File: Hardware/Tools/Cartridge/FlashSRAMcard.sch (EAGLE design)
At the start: 18 parts, among them IC1 AS29CF160B-55TIN, IC2 74LS595D, IC3 74LS244DW, IC5 74AHC1G04DBV, IC6 74AHC1G32DBV, IC7 74AHC1G32DBV

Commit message: more sram cart changes
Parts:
- added D1, D2: (no value), semicon-smd-ipc:D-MLL-34
- added R1, R2, R3: (no value), rcl:R-US_R0805
- added U$3: BATTERY2025-SMD, 0_gametankparts:BATTERY2025-SMD
- IC2: value 74LS595D -> 74HC595; device 74xx-us:74LS595D -> 0_gametankparts:74HC595
- IC3: value 74LS244DW -> 74HC244; device 74xx-us:74LS244DW -> 0_gametankparts:74HC244
- U$2: value SRAM_32KSOP28 -> SRAM_32KTSOP28; device 0_gametankparts:SRAM_32KSOP28 -> 0_gametankparts:SRAM_32KTSOP28
- renumbered VCC to IC4
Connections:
- new net N$5: D1.A, U$3.+
- new net N$6: C4.1, D1.C, D2.C, R1.1, R2.1, R3.1, U$2G$2.VCC
- net !OE: now also R1.2
- net !WE: now also R2.2
- net D0: now also U$2G$1.D0
- net D1: now also U$2G$1.D1
- net D2: now also U$2G$1.D2
- net D3: now also U$2G$1.D3
- net D4: now also U$2G$1.D4
- net D5: now also U$2G$1.D5
- net D6: now also U$2G$1.D6
- net D7: now also U$2G$1.D7
- net GND: now also U$1G$2.GND, U$2G$2.GND, U$3.-
- net N$2: now also R3.2
- net VCC: now also D2.A, U$1G$2.VCC; no longer C4.1
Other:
- moved on the sheet: C4, IC6

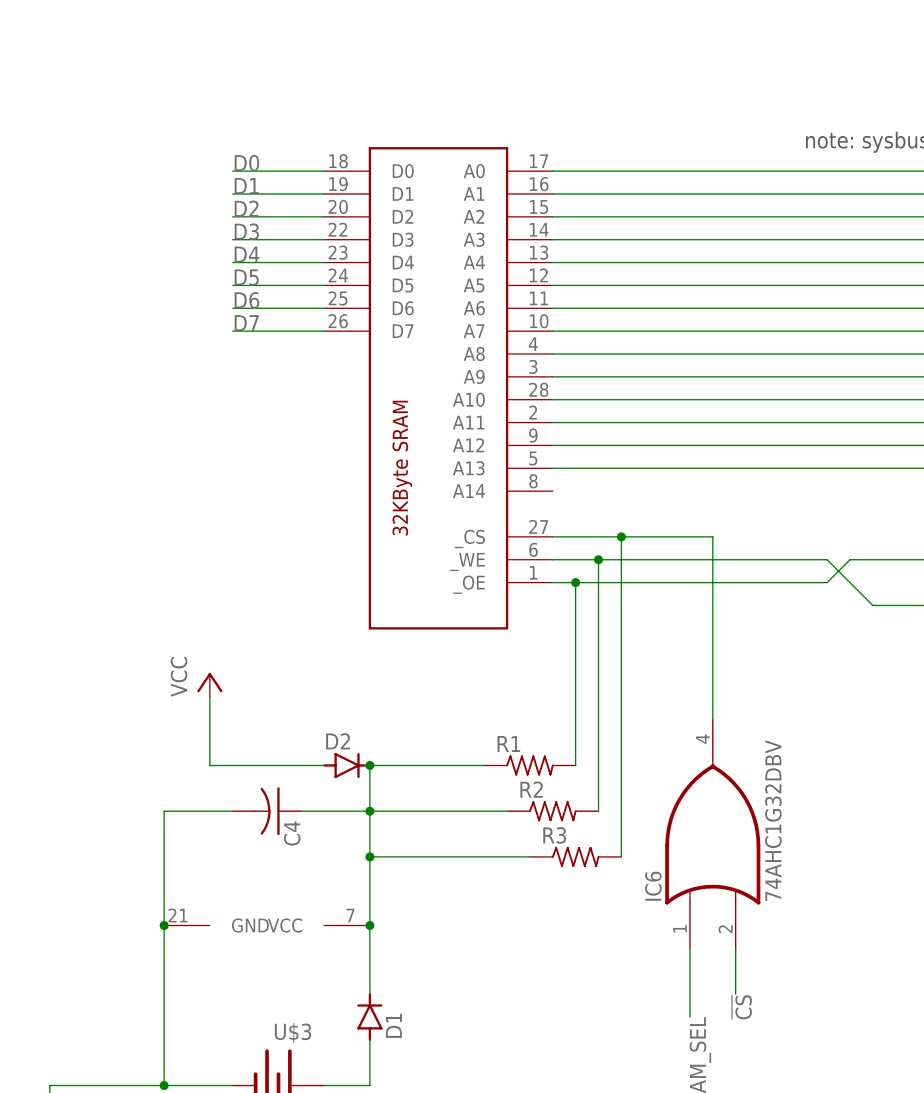
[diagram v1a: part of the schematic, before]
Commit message: RAM cartridge fixes
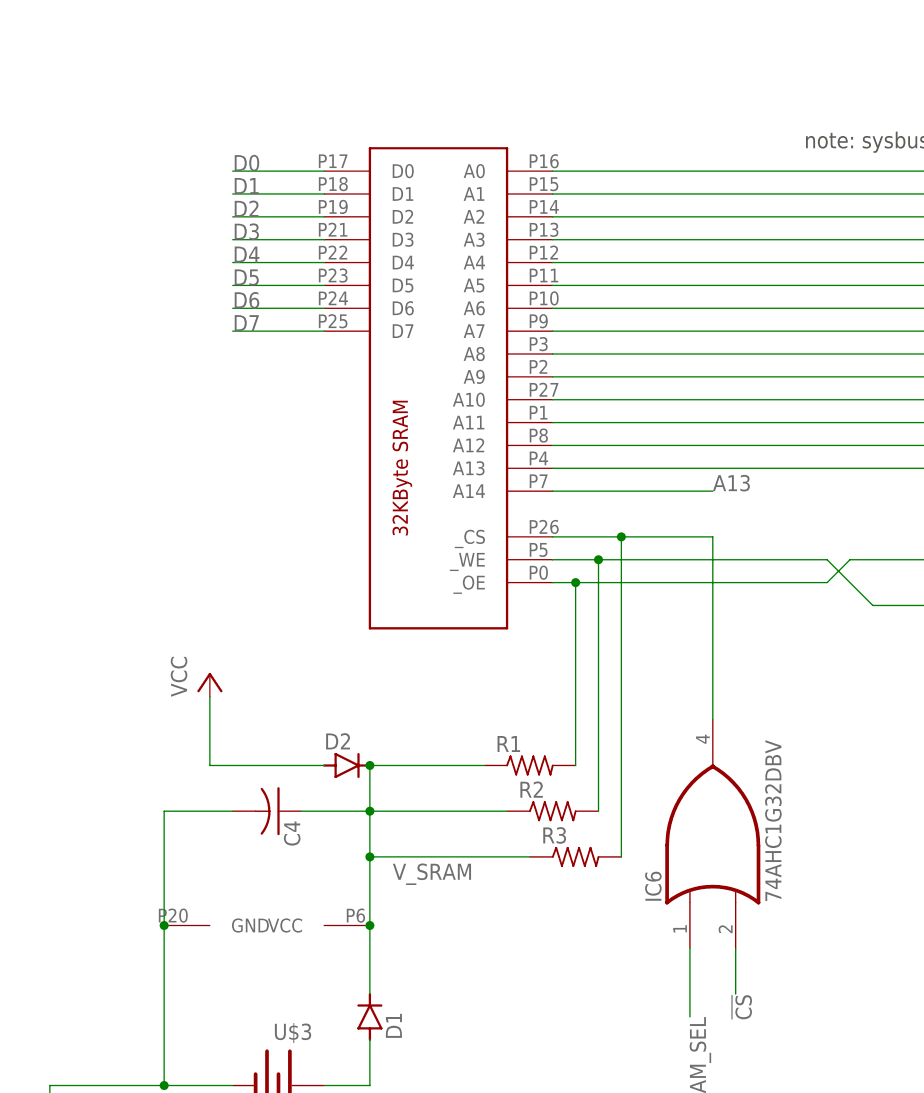
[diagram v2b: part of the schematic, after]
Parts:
- U$2: value SRAM_32KTSOP28 -> SRAM_32KALLIANCE; device 0_gametankparts:SRAM_32KTSOP28 -> 0_gametankparts:SRAM_32KALLIANCE
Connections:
- net N$6 renamed V_SRAM
- net A13: now also U$2G$1.A14
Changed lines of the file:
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@@
 <part name="P+5" library="supply1" library_urn="urn:adsk.eagle:library:371" deviceset="VCC" device=""/>
 <part name="P+4" library="supply1" library_urn="urn:adsk.eagle:library:371" deviceset="VCC" device=""/>
-<part name="U$2" library="0_gametankparts" deviceset="SRAM_32K" device="TSOP28" value="SRAM_32KTSOP28"/>
+<part name="U$2" library="0_gametankparts" deviceset="SRAM_32K" device="ALLIANCE" value="SRAM_32KALLIANCE"/>
 <part name="IC6" library="74xx-little-us" library_urn="urn:adsk.eagle:library:87" deviceset="74*1G32" device="DBV" package3d_urn="urn:adsk.eagle:package:2406/2" technology="AHC"/>
 <part name="IC7" library="74xx-little-us" library_urn="urn:adsk.eagle:library:87" deviceset="74*1G32" device="DBV" package3d_urn="urn:adsk.eagle:package:2406/2" technology="AHC"/>
@@
 <label x="93.98" y="-68.58" size="1.778" layer="95"/>
 </segment>
+<segment>
+<pinref part="U$2" gate="G$1" pin="A14"/>
+<wire x1="-132.08" y1="38.1" x2="-114.3" y2="38.1" width="0.1524" layer="91"/>
+<label x="-114.3" y="38.1" size="1.778" layer="95"/>
+</segment>
 </net>
 <net name="N$1" class="0">
@@
 </segment>
 </net>
-<net name="N$6" class="0">
+<net name="V_SRAM" class="0">
 <segment>
 <pinref part="D1" gate="G$1" pin="C"/>
@@
 <pinref part="C4" gate="G$1" pin="1"/>
 <wire x1="-160.02" y1="2.54" x2="-152.4" y2="2.54" width="0.1524" layer="91"/>
-</segment>
-</net>
+<label x="-149.86" y="-5.08" size="1.778" layer="95"/>
+</segment>
+</net>

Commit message: some SRAM cartridge stuff
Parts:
- removed W: (no value), jumper:SJ2W
- added D3, D4, D5: (no value), semicon-smd-ipc:D-MLL-34
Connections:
- removed net N$3: IC1.!WE, W.2
- new net N$6: D3.A, IC6A.O
- new net N$7: D4.C, R2.2, U$2G$1._WE
- new net N$8: D5.C, R1.2, U$2G$1._OE
- net !OE: now also D5.A; no longer R1.2, U$2G$1._OE
- net !WE: now also D4.A, IC1.!WE; no longer R2.2, U$2G$1._WE, W.1
- net N$2: now also D3.C; no longer IC6A.O
- net VCC: no longer W.3
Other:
- moved on the sheet: IC6
